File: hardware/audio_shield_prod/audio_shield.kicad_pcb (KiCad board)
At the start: 2 copper layers, 133 x 133 mm, 127 parts, among them J1 CONN_10_LEFT, J10 Conn_01x02_Male, J11 Conn_01x02_Male, J12 Conn_01x02_Male, J13 Conn_01x02_Male, J14 Conn_01x02_Male, J15 Conn_01x02_Male, J16 Conn_01x02_Male, J17 Conn_01x02_Male, J18 Conn_01x02_Male, J19 Conn_01x02_Male, J2 CONN_10_RIGHT, J20 Conn_01x02_Male, J21 Conn_01x02_Male, J22 Conn_01x02_Male, J23 Conn_01x02_Male, J24 Conn_01x02_Male, J25 Conn_01x02_Male, J26 Conn_01x02_Male, J27 Conn_01x02_Male, J28 Conn_01x02_Male, J29 Conn_01x02_Male, J3 mic_connector, J30 Conn_01x02_Male, J31 Conn_01x02_Male, J32 Conn_01x02_Male, J33 Conn_01x02_Male, J34 Conn_01x02_Male, J35 Conn_01x02_Male, J36 Conn_01x02_Male, J37 Conn_01x02_Male, J38 Conn_01x02_Male, J39 Conn_01x02_Male, J4 mic_connector, J40 Conn_01x02_Male, J41 Conn_01x02_Male, J42 Conn_01x02_Male, J43 Conn_01x02_Male, J5 mic_connector, J6 mic_connector, J7 mic_connector, J8 mic_connector, J9 SWD_TC2030, U1 STM32F446RETx

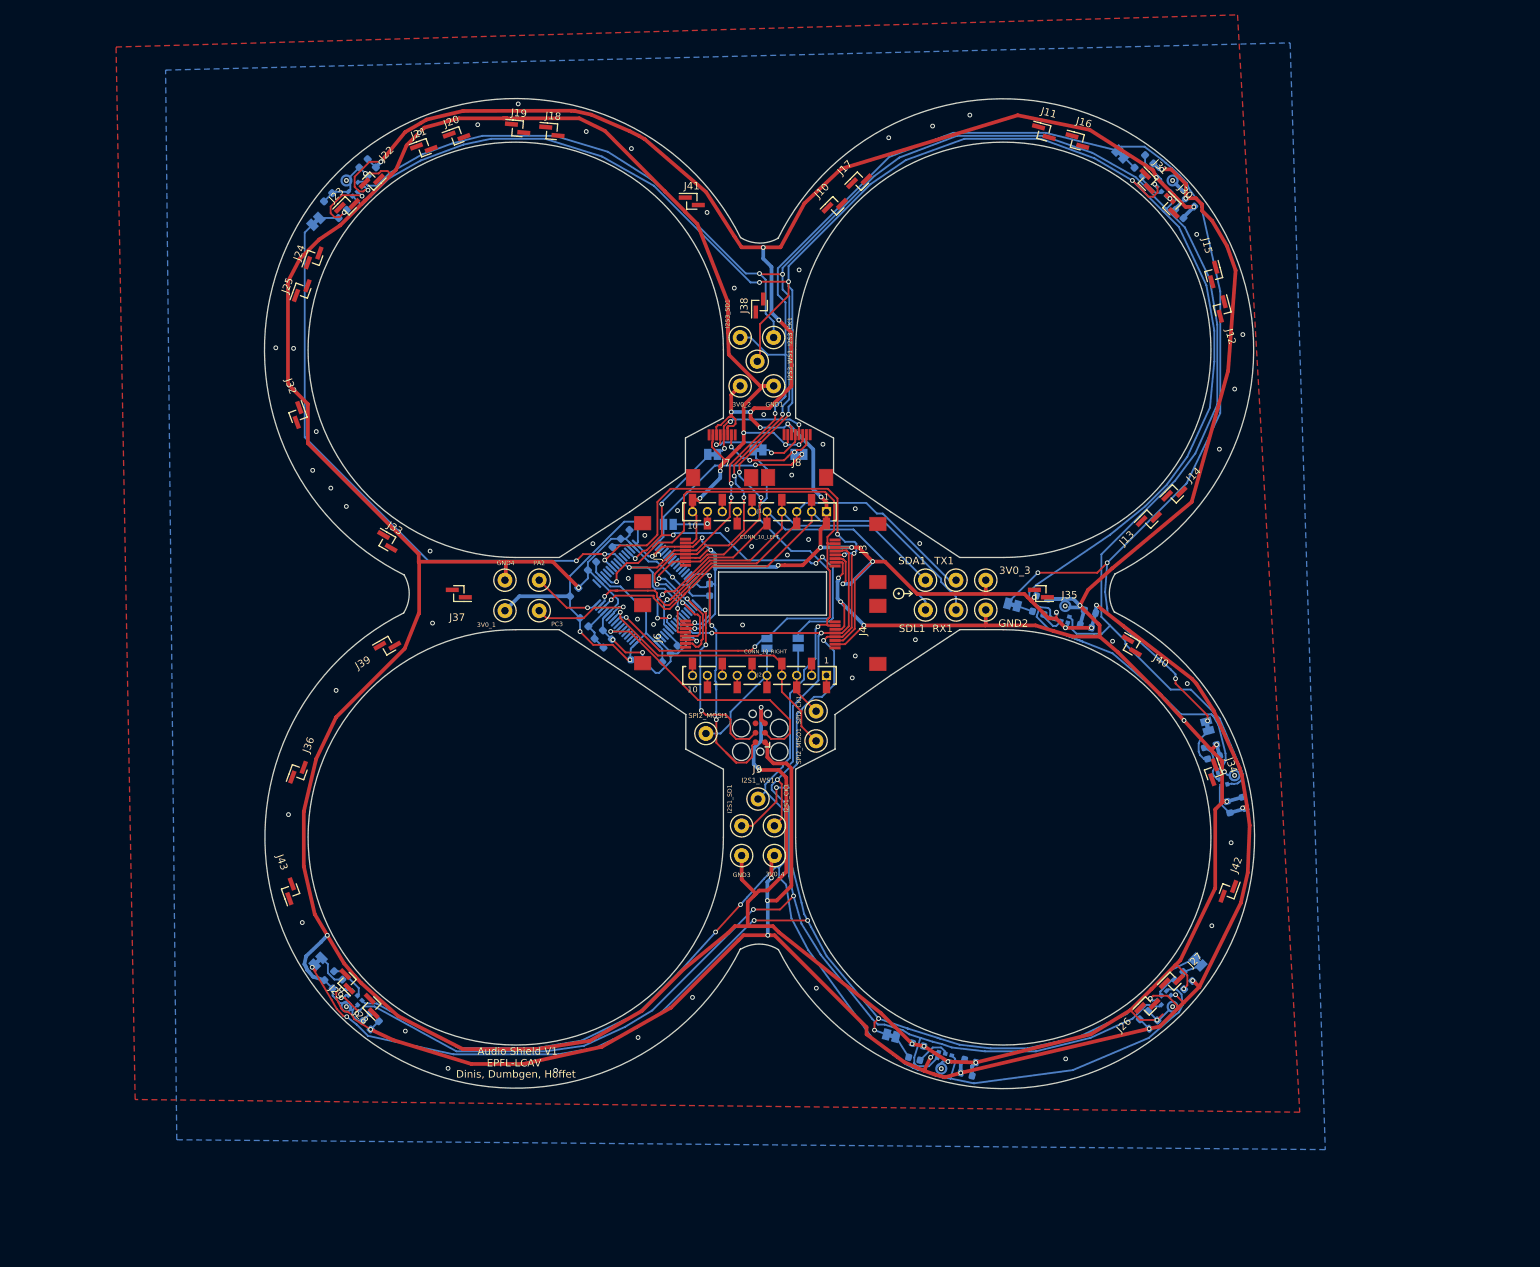
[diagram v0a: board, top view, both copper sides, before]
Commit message: flipped and changed audio deck crazyflie pins + added identification EEPROM
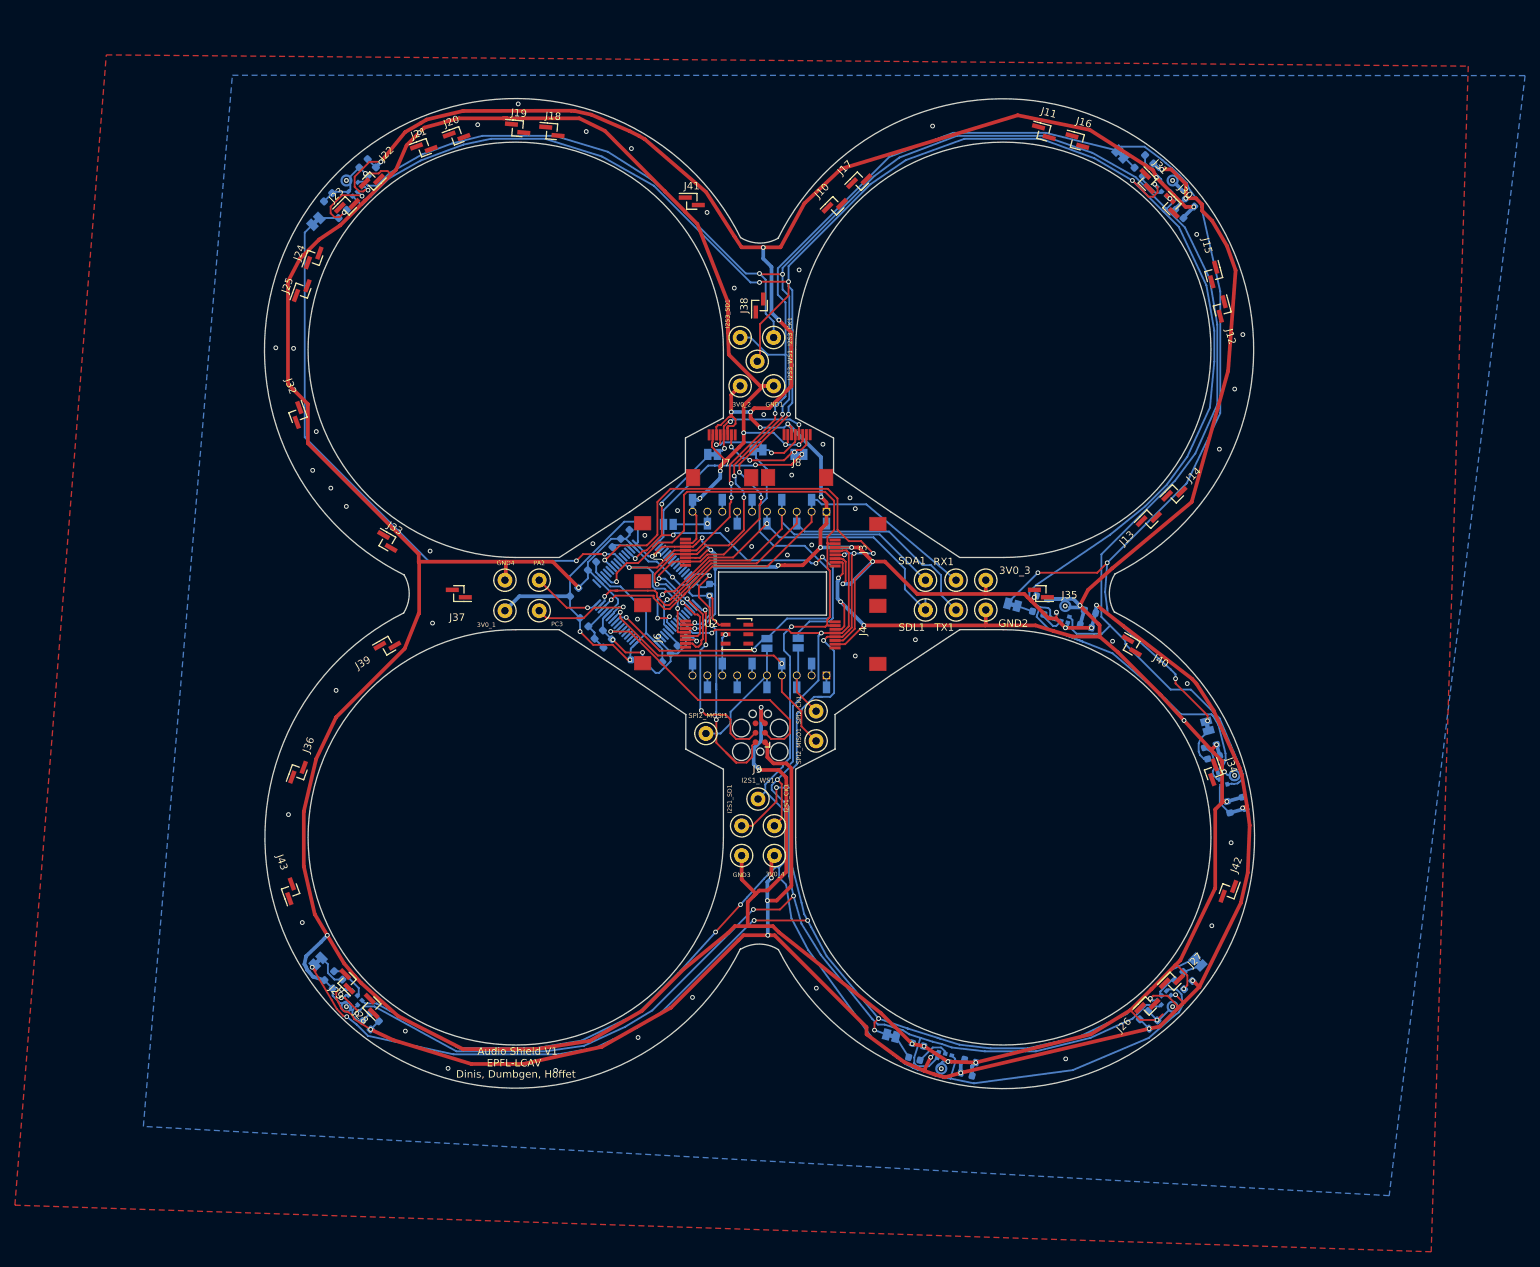
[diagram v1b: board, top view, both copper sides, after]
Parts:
- removed EXP_ORIENTATION: VAL**, audio_shield:EXP_ORIENTATION
- added U2: DS28E05P, Package_SO_J-Lead:TSOC-6_3.76x3.94mm_P1.27mm, F.Cu at (136.0, 102.5)
- J1, J2: footprint audio_shield:BF090-10-X-B2 -> audio_shield:BF090-10-X-B1; moved to B.Cu
- moved RX1 4.00 mm to (165.4, 95.2)
- moved TX1 4.00 mm to (165.4, 99.2)
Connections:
- J2 pad 8: Net-(J2-Pad8) -> /EEPROM
- J30 pad 1: +3V0 -> Net-(J30-Pad1)
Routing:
- net /EEPROM: track 0.00 -> 5.68 mm, vias 0 -> 1
- net GND: track 776.6 -> 782.0 mm, vias 86 -> 82
- net /I2S1_SD: track 263.5 -> 268.4 mm
- net /TX1: track 61.5 -> 64.7 mm
- net /RX1: track 64.2 -> 61.4 mm
- net /I2S1_WS: track 247.4 -> 250.0 mm
- net /SCL: track 54.3 -> 56.1 mm, vias 3 -> 4
- net /I2S2_SD-SPI2_MOSI: track 61.9 -> 63.6 mm
- net +3V0: track 670.0 -> 671.6 mm
- net Net-(J2-Pad8): track 1.60 -> 0.00 mm
- net /SPI2_CK: track 9.66 -> 11.3 mm
- net /SWDIO: track 36.8 -> 37.9 mm
- net /SDA: track 51.8 -> 52.5 mm
- net /I2S2_WS-SPI2_NSS: track 28.0 -> 28.6 mm
- net /SPI2_MISO: vias 1 -> 2
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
